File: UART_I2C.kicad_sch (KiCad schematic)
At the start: 13 parts, among them U10 ZX-SH1.0-4PWT, U11 ZX-SH1.0-3PWT, U9 AT7456ELAH, Y2 XL7EL89COI-111YLC-27M

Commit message: Remove unused file
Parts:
- removed C33, C34, C35, C38: 100n, Capacitor_SMD:C_0402_1005Metric, symbol Device:C_Small
- removed C36, C37: 10u, Capacitor_SMD:C_0402_1005Metric, symbol Device:C_Small
- removed R21: 10K, Resistor_SMD:R_0402_1005Metric, symbol Device:R_Small
- removed R22, R23: 75R, Resistor_SMD:R_0402_1005Metric, symbol Device:R_Small
- removed U10: ZX-SH1.0-4PWT, EasyEDA:CONN-SMD_4P-P1.00_MEGASTAR_ZX-SH1.0-4PWT, symbol EasyEDA:ZX-SH1.0-4PWT
- removed U11: ZX-SH1.0-3PWT, EasyEDA:CONN-SMD_3P-P1.00_MEGASTAR_ZX-SH1.0-3PWT, symbol EasyEDA:ZX-SH1.0-3PWT
- removed U9: AT7456ELAH, EasyEDA:LGA-16_L6.8-W4.0-P0.65-TL-2EP, symbol EasyEDA:AT7456ELAH_C42388749
- removed Y2: XL7EL89COI-111YLC-27M, Crystal:Crystal_SMD_2016-4Pin_2.0x1.6mm, symbol Device:Crystal_GND24_Small
- added C62: 10u, Capacitor_SMD:C_0805_2012Metric, symbol Device:C_Small
- added C63, C64, C65, C66, C69: 100n, Capacitor_SMD:C_0402_1005Metric, symbol Device:C_Small
- added J11, J12, J14, J4, J7: Conn_01x04, symbol Connector_Generic:Conn_01x04
- added J13: Conn_01x06, symbol Connector_Generic:Conn_01x06
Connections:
- net +5V_SYS: now also C64.1, C69.1, J11.2 (Pin_2), J14.2 (Pin_2)
- net +9V: now also C62.1, J4.1 (Pin_1)
- net GND: now also C62.2, C63.2, C64.2, C65.2, C66.2, C69.2, J11.1 (Pin_1), J12.1 (Pin_1), J13.3 (Pin_3), J14.1 (Pin_1), J4.2 (Pin_2), J7.1 (Pin_1)
- net UART1.RX: now also J7.3 (Pin_3)
- net UART1.TX: now also J7.4 (Pin_4)
- new net +5V: C63.1, C65.1, C66.1, J12.2 (Pin_2), J13.4 (Pin_4), J7.2 (Pin_2)
- new net UART2.RX: J11.3 (Pin_3)
- new net UART2.TX: J11.4 (Pin_4)
- new net UART3.RX: J12.3 (Pin_3)
- new net UART3.TX: J12.4 (Pin_4)
- new net UART4.RX: J4.4 (Pin_4)
- new net UART4.TX: J4.3 (Pin_3)
- new net UART6.RX: J14.3 (Pin_3)
- new net UART6.TX: J14.4 (Pin_4)
- new net UART7.CTS: J13.2 (Pin_2)
- new net UART7.RTS: J13.1 (Pin_1)
- new net UART7.RX: J13.5 (Pin_5)
- new net UART7.TX: J13.6 (Pin_6)
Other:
- note added: "DJI O4"
- note added: "UART1"
- note added: "UART2"
- note added: "UART3"
- note added: "UART6"
- note added: "UART7"
- note added: "UART_I2C"
- note removed: "ANALOG VTX"

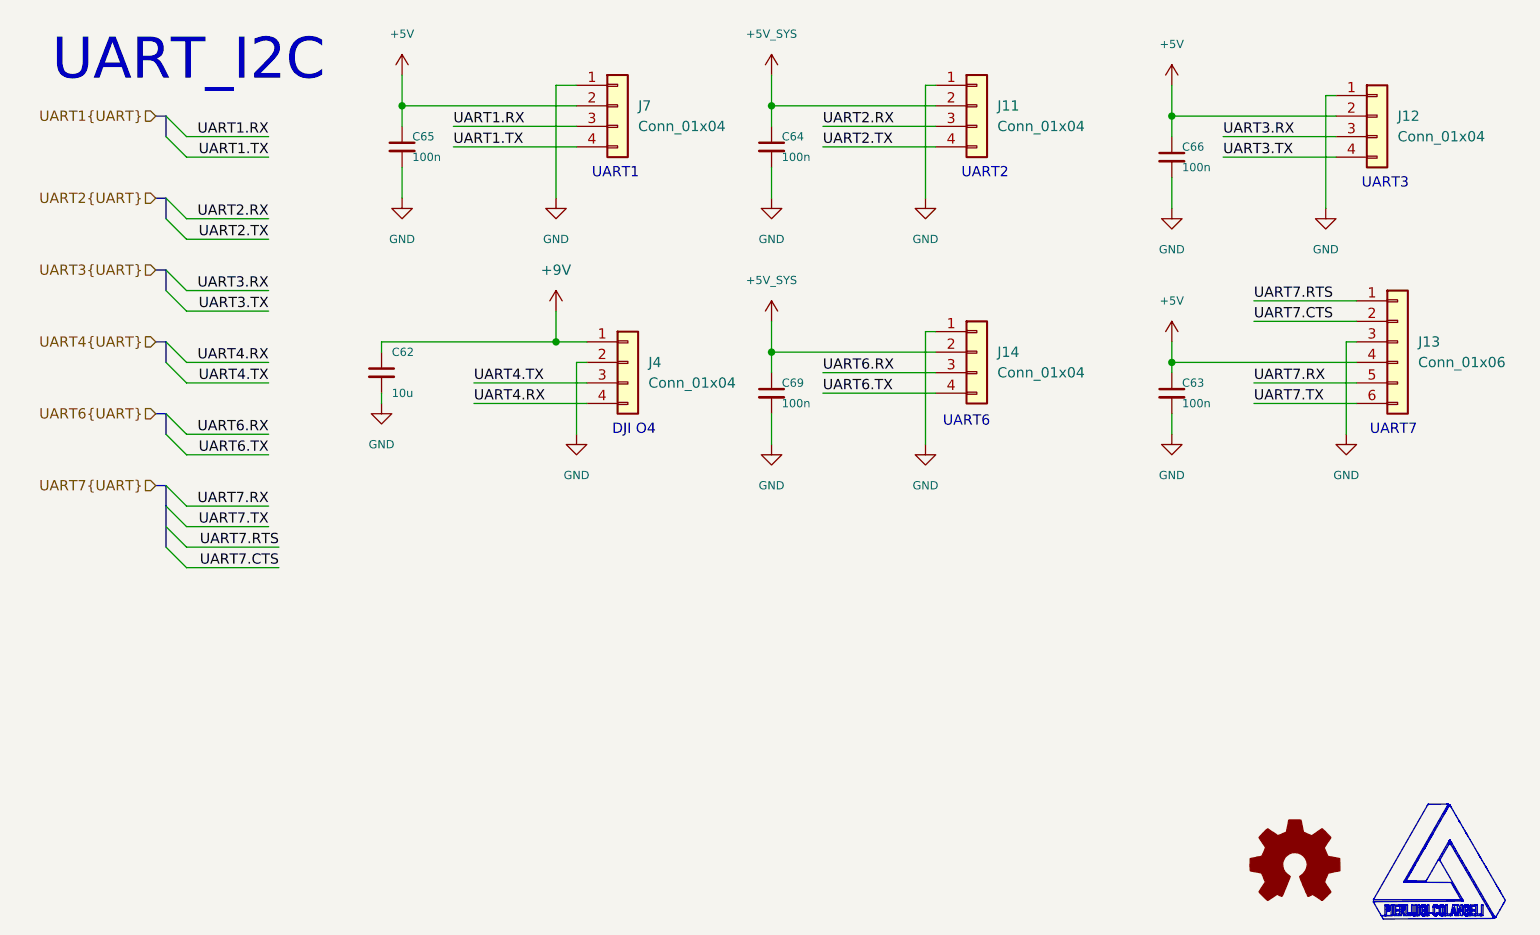
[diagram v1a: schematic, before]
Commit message: rework and work on IMUs
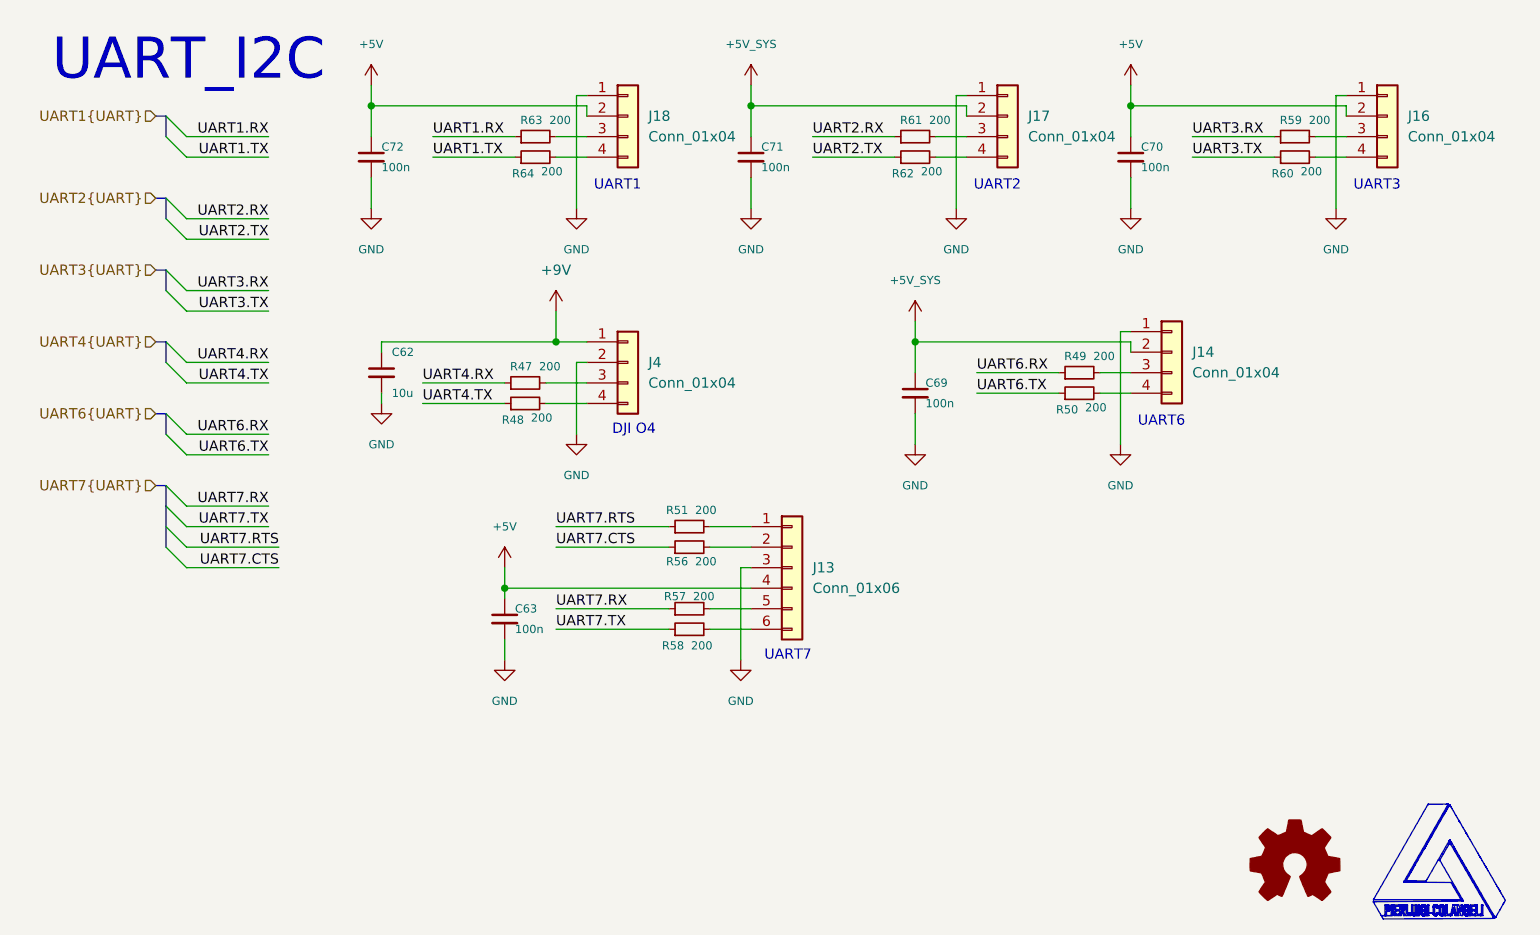
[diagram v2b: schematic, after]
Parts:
- removed C64, C65, C66: 100n, Capacitor_SMD:C_0402_1005Metric, symbol Device:C_Small
- removed J11, J12, J7: Conn_01x04, symbol Connector_Generic:Conn_01x04
- added C70, C71, C72: 100n, Capacitor_SMD:C_0402_1005Metric, symbol Device:C_Small
- added J16, J17, J18: Conn_01x04, symbol Connector_Generic:Conn_01x04
- added R47, R48, R49, R50, R51, R56, R57, R58, R59, R60, R61, R62, R63, R64: 200, Resistor_SMD:R_0402_1005Metric, symbol Device:R_Small
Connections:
- net +5V: now also C70.1, C72.1, J16.2 (Pin_2), J18.2 (Pin_2)
- net +5V_SYS: now also C71.1, J17.2 (Pin_2)
- net GND: now also C70.2, C71.2, C72.2, J16.1 (Pin_1), J17.1 (Pin_1), J18.1 (Pin_1)
- net UART1.RX: now also R63.1
- net UART1.TX: now also R64.1
- net UART2.RX: now also R61.1
- net UART2.TX: now also R62.1
- net UART3.RX: now also R59.1
- net UART3.TX: now also R60.1
- net UART4.RX: now also R47.1; no longer J4.4 (Pin_4)
- net UART4.TX: now also R48.1; no longer J4.3 (Pin_3)
- net UART6.RX: now also R49.1; no longer J14.3 (Pin_3)
- net UART6.TX: now also R50.1; no longer J14.4 (Pin_4)
- net UART7.CTS: now also R56.1; no longer J13.2 (Pin_2)
- net UART7.RTS: now also R51.1; no longer J13.1 (Pin_1)
- net UART7.RX: now also R57.1; no longer J13.5 (Pin_5)
- net UART7.TX: now also R58.1; no longer J13.6 (Pin_6)
- new net: J4.3 (Pin_3), R47.2
- new net: J13.1 (Pin_1), R51.2
- new net: J17.3 (Pin_3), R61.2
- new net: J17.4 (Pin_4), R62.2
- new net: J13.5 (Pin_5), R57.2
- new net: J16.4 (Pin_4), R60.2
- new net: J14.3 (Pin_3), R49.2
- new net: J18.3 (Pin_3), R63.2
- new net: J14.4 (Pin_4), R50.2
- new net: J13.6 (Pin_6), R58.2
- new net: J4.4 (Pin_4), R48.2
- new net: J16.3 (Pin_3), R59.2
- new net: J13.2 (Pin_2), R56.2
- new net: J18.4 (Pin_4), R64.2
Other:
- moved on the sheet: C63, C69, J13, J14

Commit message: update name
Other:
- note removed: "UART_I2C"
- company: Pierluigi Colangeli, PhD -> (none)
- title: LEVIA H7 -> (none)

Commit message: upsadte SPI4 set to Baro
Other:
- title: (none) -> H743_ARDUPILOT
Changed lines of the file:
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@@
 	(generator "eeschema")
 	(generator_version "10.0")
-	(paper "A5")
+	(paper "A3")
 	(title_block
+		(title "H743_ARDUPILOT")
 		(date "2026-09-24")
 	)

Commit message: re annotate componant globaly
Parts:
- renumbered C72 to C19, C62 to C20, C63 to C21, C71 to C22, C69 to C23, C70 to C24, J18 to J2, J4 to J3, J13 to J4, J17 to J5, J14 to J6, J16 to J7, R47 to R14, R48 to R15, R63 to R16, R64 to R17, R51 to R18, R56 to R19, R57 to R20, R58 to R21, R61 to R22, R62 to R23, R49 to R24, R50 to R25, R59 to R26, R60 to R27

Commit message: audit DigiKey metadata: UART_I2C.kicad_sch
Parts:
- C19, C21, C22, C23, C24: DigiKey Part Number (none) -> 1276-1001-1-ND; DigiKey Price Qty (none) -> 1 CT; DigiKey Specs (none) -> 100 nF ±10%, 16 V, X7R, 0402; DigiKey Status (none) -> Active; DigiKey URL (none) -> https://www.digikey.fr/fr/products/detail/samsung-electro-m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; DigiKey Unit Price EUR (none) -> 0.09; Footprint Audit (none) -> OK; LCSC C1525 -> (none); LCSC Part C1525 -> (none); Library Audit (none) -> KiCad standard; MPN GRM022R60J104KE15D -> CL05B104KO5NNNC; Manufacturer Murata Electronics -> Samsung Electro-Mechanics; Package (none) -> 0402 (1005); Price Checked (none) -> 2026-09-25
- C20: DigiKey Part Number (none) -> 490-18663-1-ND; DigiKey Price Qty (none) -> 1 CT; DigiKey Specs (none) -> 10 µF ±10%, 50 V, X5R, 0805; DigiKey Status (none) -> Active; DigiKey URL (none) -> https://www.digikey.fr/fr/products/detail/murata-electronic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; DigiKey Unit Price EUR (none) -> 0.28; Footprint Audit (none) -> OK; LCSC C45783 -> (none); LCSC Part C45783 -> (none); Library Audit (none) -> KiCad standard; MPN CL21A226MAQNNNE -> GRM21BR61H106KE43L; Manufacturer Samsung Electro-Mechanics -> Murata Electronics; Package (none) -> 0805 (2012); Price Checked (none) -> 2026-09-25
- J2, J3, J4, J5, J6, J7: DigiKey Status (none) -> TBD: connector not physically selected; Footprint Audit (none) -> BLOCKING: no footprint assigned; Library Audit (none) -> Generic KiCad connector; Package (none) -> TBD; Price Checked (none) -> 2026-09-25
- R14, R15, R16, R17, R18, R19, R20, R21, R22, R23, R24, R25, R26, R27: DigiKey Specs (none) -> 200 ±1%, 0402 (1005), thick film; DigiKey Status (none) -> Active / DigiKey family verified; DigiKey URL (none) -> https://www.digikey.fr/en/products/result?keywords=RC0402FR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; Footprint Audit (none) -> OK; LCSC C25744 -> (none); LCSC Part C25744 -> (none); Library Audit (none) -> KiCad standard; MPN 0402WGF1002TCE -> RC0402FR-07200RL; Manufacturer UNI-ROYAL(Uniroyal Elec) -> YAGEO; Package (none) -> 0402 (1005 Metric); Price Checked (none) -> 2026-09-25

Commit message: assign Matek-style solder pad footprints in UART_I2C.kicad_sch
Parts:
- J2, J3, J5, J6, J7: footprint (none) -> H743_Custom:SolderPadArray_1x04_P2.54mm_1x1mm; DigiKey Status TBD: connector not physically selected -> PCB feature / no purchased component; Footprint Audit BLOCKING: no footprint assigned -> OK: 4 square SMD pads 1.00x1.00 mm, P2.54 mm, no holes, no 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; Library Audit Generic KiCad connector -> Project-local H743_Custom footprint; Package TBD -> Solder pad array 1x4, P2.54 mm, 1.00x1.00 mm SMD
- J4: footprint (none) -> H743_Custom:SolderPadArray_1x06_P2.54mm_1x1mm; DigiKey Status TBD: connector not physically selected -> PCB feature / no purchased component; Footprint Audit BLOCKING: no footprint assigned -> OK: 6 square SMD pads 1.00x1.00 mm, P2.54 mm, no holes, no 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; Library Audit Generic KiCad connector -> Project-local H743_Custom footprint; Package TBD -> Solder pad array 1x6, P2.54 mm, 1.00x1.00 mm SMD
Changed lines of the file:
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@@
 			)
 		)
-		(property "Footprint" ""
+		(property "Footprint" "H743_Custom:SolderPadArray_1x04_P2.54mm_1x1mm"
 			(at 134.62 25.4 0)
 			(hide yes)
@@
 			)
 		)
-		(property "DigiKey Status" "TBD: connector not physically selected"
+		(property "DigiKey Status" "PCB feature / no purchased component"
 			(at 137.16 25.3999 0)
 			(hide yes)
@@
 			)
 		)
-		(property "Package" "TBD"
+		(property "Package" "Solder pad array 1x4, P2.54 mm, 1.00x1.00 mm SMD"
 			(at 137.16 25.3999 0)
 			(hide yes)
@@
 			)
 		)
-		(property "Footprint Audit" "BLOCKING: no footprint assigned"
+		(property "Footprint Audit" "OK: 4 square SMD pads 1.00x1.00 mm, P2.54 mm, no holes, no paste"
 			(at 137.16 25.3999 0)
 			(hide yes)
@@
 			)
 		)
-		(property "Library Audit" "Generic KiCad connector"
+		(property "Library Audit" "Project-local H743_Custom footprint"
 			(at 137.16 25.3999 0)
 			(hide yes)
@@
 			)
 		)
-		(property "Footprint" ""
+		(property "Footprint" "H743_Custom:SolderPadArray_1x04_P2.54mm_1x1mm"
 			(at 154.94 54.61 0)
 			(hide yes)
@@
 			)
 		)
-		(property "DigiKey Status" "TBD: connector not physically selected"
+		(property "DigiKey Status" "PCB feature / no purchased component"
 			(at 157.48 54.6099 0)
 			(hide yes)
@@
 			)
 		)
-		(property "Package" "TBD"
+		(property "Package" "Solder pad array 1x4, P2.54 mm, 1.00x1.00 mm SMD"
 			(at 157.48 54.6099 0)
 			(hide yes)
@@
 			)
 		)
-		(property "Footprint Audit" "BLOCKING: no footprint assigned"
+		(property "Footprint Audit" "OK: 4 square SMD pads 1.00x1.00 mm, P2.54 mm, no holes, no paste"
 			(at 157.48 54.6099 0)
 			(hide yes)
@@
 			)
 		)
-		(property "Library Audit" "Generic KiCad connector"
+		(property "Library Audit" "Project-local H743_Custom footprint"
 			(at 157.48 54.6099 0)
 			(hide yes)
@@
 			)
 		)
-		(property "Footprint" ""
+		(property "Footprint" "H743_Custom:SolderPadArray_1x04_P2.54mm_1x1mm"
 			(at 87.63 55.88 0)
 			(hide yes)
@@
 			)
 		)
-		(property "DigiKey Status" "TBD: connector not physically selected"
+		(property "DigiKey Status" "PCB feature / no purchased component"
 			(at 90.17 55.8799 0)
 			(hide yes)
@@
 			)
 		)
-		(property "Package" "TBD"
+		(property "Package" "Solder pad array 1x4, P2.54 mm, 1.00x1.00 mm SMD"
 			(at 90.17 55.8799 0)
 			(hide yes)
@@
 			)
 		)
-		(property "Footprint Audit" "BLOCKING: no footprint assigned"
+		(property "Footprint Audit" "OK: 4 square SMD pads 1.00x1.00 mm, P2.54 mm, no holes, no paste"
 			(at 90.17 55.8799 0)
 			(hide yes)
@@
 			)
 		)
-		(property "Library Audit" "Generic KiCad connector"
+		(property "Library Audit" "Project-local H743_Custom footprint"
 			(at 90.17 55.8799 0)
 			(hide yes)
@@
 			)
 		)
-		(property "Footprint" ""
+		(property "Footprint" "H743_Custom:SolderPadArray_1x04_P2.54mm_1x1mm"
 			(at 181.61 25.4 0)
 			(hide yes)
@@
 			)
 		)
-		(property "DigiKey Status" "TBD: connector not physically selected"
+		(property "DigiKey Status" "PCB feature / no purchased component"
 			(at 184.15 25.3999 0)
 			(hide yes)
@@
 			)
 		)
-		(property "Package" "TBD"
+		(property "Package" "Solder pad array 1x4, P2.54 mm, 1.00x1.00 mm SMD"
 			(at 184.15 25.3999 0)
 			(hide yes)
@@
 			)
 		)
-		(property "Footprint Audit" "BLOCKING: no footprint assigned"
+		(property "Footprint Audit" "OK: 4 square SMD pads 1.00x1.00 mm, P2.54 mm, no holes, no paste"
 			(at 184.15 25.3999 0)
 			(hide yes)
@@
 			)
 		)
-		(property "Library Audit" "Generic KiCad connector"
+		(property "Library Audit" "Project-local H743_Custom footprint"
 			(at 184.15 25.3999 0)
 			(hide yes)
@@
 			)
 		)
-		(property "Footprint" ""
+		(property "Footprint" "H743_Custom:SolderPadArray_1x04_P2.54mm_1x1mm"
 			(at 87.63 25.4 0)
 			(hide yes)
@@
 			)
 		)
-		(property "DigiKey Status" "TBD: connector not physically selected"
+		(property "DigiKey Status" "PCB feature / no purchased component"
 			(at 90.17 25.3999 0)
 			(hide yes)
@@
 			)
 		)
-		(property "Package" "TBD"
+		(property "Package" "Solder pad array 1x4, P2.54 mm, 1.00x1.00 mm SMD"
 			(at 90.17 25.3999 0)
 			(hide yes)
@@
 			)
 		)
-		(property "Footprint Audit" "BLOCKING: no footprint assigned"
+		(property "Footprint Audit" "OK: 4 square SMD pads 1.00x1.00 mm, P2.54 mm, no holes, no paste"
 			(at 90.17 25.3999 0)
 			(hide yes)
@@
 			)
 		)
-		(property "Library Audit" "Generic KiCad connector"
+		(property "Library Audit" "Project-local H743_Custom footprint"
 			(at 90.17 25.3999 0)
 			(hide yes)
@@
 			)
 		)
-		(property "Footprint" ""
+		(property "Footprint" "H743_Custom:SolderPadArray_1x06_P2.54mm_1x1mm"
 			(at 107.95 81.28 0)
 			(hide yes)
@@
 			)
 		)
-		(property "DigiKey Status" "TBD: connector not physically selected"
+		(property "DigiKey Status" "PCB feature / no purchased component"
 			(at 110.49 81.2799 0)
 			(hide yes)
@@
 			)
 		)
-		(property "Package" "TBD"
+		(property "Package" "Solder pad array 1x6, P2.54 mm, 1.00x1.00 mm SMD"
 			(at 110.49 81.2799 0)
 			(hide yes)
@@
 			)
 		)
-		(property "Footprint Audit" "BLOCKING: no footprint assigned"
+		(property "Footprint Audit" "OK: 6 square SMD pads 1.00x1.00 mm, P2.54 mm, no holes, no paste"
 			(at 110.49 81.2799 0)
 			(hide yes)
@@
 			)
 		)
-		(property "Library Audit" "Generic KiCad connector"
+		(property "Library Audit" "Project-local H743_Custom footprint"
 			(at 110.49 81.2799 0)
 			(hide yes)
